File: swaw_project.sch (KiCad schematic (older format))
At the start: 9 parts, among them P1 Power, P2 Analog, P3 Digital, P4 Digital, P5 CONN_01X01, P6 CONN_01X01, P7 CONN_01X01, P8 CONN_01X01

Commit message: Add files via upload
Bluetooth module scheme added to the library of project
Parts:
- added B:HC-05?: Bluetooth_HC-05, symbol swaw_project-cache:Bluetooth_HC-05
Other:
- moved on the sheet: U?
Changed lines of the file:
@@
 L Sensor_Motion:MPU-6050 U?
 U 1 1 5EA88EF4
-P 2900 2150
-F 0 "U?" H 2900 1361 50  0000 C CNN
-F 1 "MPU-6050" H 2900 1270 50  0000 C CNN
-F 2 "Sensor_Motion:InvenSense_QFN-24_4x4mm_P0.5mm" H 2900 1350 50  0001 C CNN
-F 3 "https://store.invensense.com/datasheets/invensense/MPU-6050_DataSheet_V3%204.pdf" H 2900 2000 50  0001 C CNN
-	1    2900 2150
+P 2700 2050
+F 0 "U?" H 2700 1261 50  0000 C CNN
+F 1 "MPU-6050" H 2700 1170 50  0000 C CNN
+F 2 "Sensor_Motion:InvenSense_QFN-24_4x4mm_P0.5mm" H 2700 1250 50  0001 C CNN
+F 3 "https://store.invensense.com/datasheets/invensense/MPU-6050_DataSheet_V3%204.pdf" H 2700 1900 50  0001 C CNN
+	1    2700 2050
 	1    0    0    -1
 $EndComp
+$Comp
+L swaw_project-cache:Bluetooth_HC-05 B:HC-05?
+U 1 1 5EAA6265
+P 5000 2400
+F 0 "B:HC-05?" H 5200 3315 50  0000 C CNN
+F 1 "Bluetooth_HC-05" H 5200 3224 50  0000 C CNN
+F 2 "" H 5000 2400 50  0001 C CNN
+F 3 "" H 5000 2400 50  0001 C CNN
+	1    5000 2400
+	1    0    0    -1
+$EndComp

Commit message: Add files via upload
Adding Bluetooth PIO, capacitors, resistors values and footprints
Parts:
- removed B:HC-05?: Bluetooth_HC-05, symbol swaw_project-cache:Bluetooth_HC-05
- added C1: 10nF, Capacitor_THT:CP_Axial_L11.0mm_D6.0mm_P18.00mm_Horizontal, symbol pspice:C
- added C2, C3: 0.1uF, Capacitor_THT:CP_Axial_L11.0mm_D6.0mm_P18.00mm_Horizontal, symbol pspice:C
- added C4: 2.2nF, Capacitor_THT:CP_Axial_L11.0mm_D6.0mm_P18.00mm_Horizontal, symbol pspice:C
- added HC-05_PIO?: Bluetooh_PIO, Connector_PinHeader_2.54mm:PinHeader_1x06_P2.54mm_Vertical, symbol Relay:Bluetooh_PIO
- added R1, R2: 10kΩ, Resistor_THT:R_Axial_DIN0309_L9.0mm_D3.2mm_P15.24mm_Horizontal, symbol Device:R
- added R3: 2kΩ, Resistor_THT:R_Axial_DIN0309_L9.0mm_D3.2mm_P15.24mm_Horizontal, symbol Device:R
- added R4: 1kΩ, Resistor_THT:R_Axial_DIN0309_L9.0mm_D3.2mm_P15.24mm_Horizontal, symbol Device:R
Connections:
- wire segments 38 -> 98
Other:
- moved on the sheet: U?

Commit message: Added logic shifters for i2c and basic pcb layout
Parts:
- added Q1, Q2: 2N7000, Package_TO_SOT_THT:TO-92_Inline, symbol Transistor_FET:2N7000
- added R5, R6: 10kΩ, Resistor_SMD:R_0612_1632Metric_Pad1.18x3.40mm_HandSolder, symbol Device:R
- C1: footprint Capacitor_THT:CP_Axial_L11.0mm_D6.0mm_P18.00mm_Horizontal -> Capacitor_SMD:C_0805_2012Metric_Pad1.15x1.40mm_HandSolder
- C2, C3: footprint Capacitor_THT:CP_Axial_L11.0mm_D6.0mm_P18.00mm_Horizontal -> Capacitor_SMD:C_1206_3216Metric_Pad1.42x1.75mm_HandSolder
- C4: footprint Capacitor_THT:CP_Axial_L11.0mm_D6.0mm_P18.00mm_Horizontal -> Capacitor_SMD:C_0603_1608Metric_Pad1.05x0.95mm_HandSolder
- HC-05_PIO1: renamed from HC-05_PIO?; symbol Relay:Bluetooh_PIO -> swaw_project-rescue:Bluetooh_PIO-Relay
- R1, R2: footprint Resistor_THT:R_Axial_DIN0309_L9.0mm_D3.2mm_P15.24mm_Horizontal -> Resistor_SMD:R_0612_1632Metric_Pad1.18x3.40mm_HandSolder
- R3: footprint Resistor_THT:R_Axial_DIN0309_L9.0mm_D3.2mm_P15.24mm_Horizontal -> Resistor_SMD:R_0805_2012Metric_Pad1.15x1.40mm_HandSolder
- R4: footprint Resistor_THT:R_Axial_DIN0309_L9.0mm_D3.2mm_P15.24mm_Horizontal -> Resistor_SMD:R_0603_1608Metric_Pad1.05x0.95mm_HandSolder
- gave numbers to parts that had none: 1
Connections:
- wire segments 98 -> 112
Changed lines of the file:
@@
 	10200 1200 10550 1200
-Wire Wire Line
-	10200 3000 10400 3000
 Wire Wire Line
 	10200 2800 10550 2800
@@
 	10700 1000 10700 500
 $Comp
-L Sensor_Motion:MPU-6050 U?
+L Sensor_Motion:MPU-6050 U1
 U 1 1 5EA88EF4
 P 2900 2150
-F 0 "U?" H 2900 1361 50  0000 C CNN
+F 0 "U1" H 2900 1361 50  0000 C CNN
 F 1 "MPU-6050" H 2900 1270 50  0000 C CNN
 F 2 "Sensor_Motion:InvenSense_QFN-24_4x4mm_P0.5mm" H 2900 1350 50  0001 C CNN
@@
 F 0 "C2" H 4078 1646 50  0000 L CNN
 F 1 "0.1uF" H 4078 1555 50  0000 L CNN
-F 2 "Capacitor_THT:CP_Axial_L11.0mm_D6.0mm_P18.00mm_Horizontal" H 3900 1600 50  0001 C CNN
+F 2 "Capacitor_SMD:C_1206_3216Metric_Pad1.42x1.75mm_HandSolder" H 3900 1600 50  0001 C CNN
 F 3 "~" H 3900 1600 50  0001 C CNN
 	1    3900 1600
@@
 	2900 900  2800 900
 $Comp
-L power:GND #PWR?
+L power:GND #PWR08
 U 1 1 5EAAFEC1
 P 3900 1850
-F 0 "#PWR?" H 3900 1600 50  0001 C CNN
+F 0 "#PWR08" H 3900 1600 50  0001 C CNN
 F 1 "GND" H 3905 1677 50  0000 C CNN
 F 2 "" H 3900 1850 50  0001 C CNN
@@
 $EndComp
 $Comp
-L power:GND #PWR?
+L power:GND #PWR06
 U 1 1 5EAB0D0F
 P 2900 1400
-F 0 "#PWR?" H 2900 1150 50  0001 C CNN
+F 0 "#PWR06" H 2900 1150 50  0001 C CNN
 F 1 "GND" H 2905 1227 50  0000 C CNN
 F 2 "" H 2900 1400 50  0001 C CNN
@@
 F 0 "C1" H 3078 1196 50  0000 L CNN
 F 1 "10nF" H 3078 1105 50  0000 L CNN
-F 2 "Capacitor_THT:CP_Axial_L11.0mm_D6.0mm_P18.00mm_Horizontal" H 2900 1150 50  0001 C CNN
+F 2 "Capacitor_SMD:C_0805_2012Metric_Pad1.15x1.40mm_HandSolder" H 2900 1150 50  0001 C CNN
 F 3 "~" H 2900 1150 50  0001 C CNN
 	1    2900 1150
@@
 $EndComp
 $Comp
-L power:GND #PWR?
+L power:GND #PWR07
 U 1 1 5EABDA5F
 P 2900 2850
-F 0 "#PWR?" H 2900 2600 50  0001 C CNN
+F 0 "#PWR07" H 2900 2600 50  0001 C CNN
 F 1 "GND" H 2905 2677 50  0000 C CNN
 F 2 "" H 2900 2850 50  0001 C CNN
@@
 F 0 "C4" H 4778 2646 50  0000 L CNN
 F 1 "2.2nF" H 4778 2555 50  0000 L CNN
-F 2 "Capacitor_THT:CP_Axial_L11.0mm_D6.0mm_P18.00mm_Horizontal" H 4600 2600 50  0001 C CNN
+F 2 "Capacitor_SMD:C_0603_1608Metric_Pad1.05x0.95mm_HandSolder" H 4600 2600 50  0001 C CNN
 F 3 "~" H 4600 2600 50  0001 C CNN
 	1    4600 2600
@@
 F 0 "C3" H 4078 2746 50  0000 L CNN
 F 1 "0.1uF" H 4078 2655 50  0000 L CNN
-F 2 "Capacitor_THT:CP_Axial_L11.0mm_D6.0mm_P18.00mm_Horizontal" H 3900 2700 50  0001 C CNN
+F 2 "Capacitor_SMD:C_1206_3216Metric_Pad1.42x1.75mm_HandSolder" H 3900 2700 50  0001 C CNN
 F 3 "~" H 3900 2700 50  0001 C CNN
 	1    3900 2700
@@
 	3900 2450 3600 2450
 $Comp
-L power:GND #PWR?
+L power:GND #PWR09
 U 1 1 5EAC0805
 P 3900 2950
-F 0 "#PWR?" H 3900 2700 50  0001 C CNN
+F 0 "#PWR09" H 3900 2700 50  0001 C CNN
 F 1 "GND" H 3905 2777 50  0000 C CNN
 F 2 "" H 3900 2950 50  0001 C CNN
@@
 $EndComp
 $Comp
-L power:GND #PWR?
+L power:GND #PWR010
 U 1 1 5EAC0AA7
 P 4600 2850
-F 0 "#PWR?" H 4600 2600 50  0001 C CNN
+F 0 "#PWR010" H 4600 2600 50  0001 C CNN
 F 1 "GND" H 4605 2677 50  0000 C CNN
 F 2 "" H 4600 2850 50  0001 C CNN
@@
 	1650 1950 2200 1950
 $Comp
-L power:GND #PWR?
+L power:GND #PWR05
 U 1 1 5EADDE16
 P 1950 2550
-F 0 "#PWR?" H 1950 2300 50  0001 C CNN
+F 0 "#PWR05" H 1950 2300 50  0001 C CNN
 F 1 "GND" H 1955 2377 50  0000 C CNN
 F 2 "" H 1950 2550 50  0001 C CNN
@@
 F 0 "R2" H 5770 1746 50  0000 L CNN
 F 1 "10kΩ" H 5770 1655 50  0000 L CNN
-F 2 "Resistor_THT:R_Axial_DIN0309_L9.0mm_D3.2mm_P15.24mm_Horizontal" V 5630 1700 50  0001 C CNN
+F 2 "Resistor_SMD:R_0612_1632Metric_Pad1.18x3.40mm_HandSolder" V 5630 1700 50  0001 C CNN
 F 3 "~" H 5700 1700 50  0001 C CNN
 	1    5700 1700
@@
 F 0 "R1" H 5320 1746 50  0000 L CNN
 F 1 "10kΩ" H 5320 1655 50  0000 L CNN
-F 2 "Resistor_THT:R_Axial_DIN0309_L9.0mm_D3.2mm_P15.24mm_Horizontal" V 5180 1700 50  0001 C CNN
+F 2 "Resistor_SMD:R_0612_1632Metric_Pad1.18x3.40mm_HandSolder" V 5180 1700 50  0001 C CNN
 F 3 "~" H 5250 1700 50  0001 C CNN
 	1    5250 1700
@@
 Connection ~ 5700 900
 Wire Wire Line
-	5700 900  9150 900
-Wire Wire Line
 	10200 1300 10700 1300
 Wire Wire Line
@@
 	1450 4050 5250 4050
 Wire Wire Line
-	5250 4050 5250 2700
-Wire Wire Line
 	1650 1950 1650 3900
 Wire Wire Line
 	1650 3900 5700 3900
 Wire Wire Line
-	5700 3900 5700 2000
-Wire Wire Line
 	10550 1200 10550 950
-Wire Wire Line
-	10550 950  6450 950
-Wire Wire Line
-	6450 950  6450 2000
-Wire Wire Line
-	6450 2000 5700 2000
-Connection ~ 5700 2000
-Wire Wire Line
-	5700 2000 5700 1850
-Wire Wire Line
-	10700 1300 10700 1050
-Wire Wire Line
-	10700 1050 6600 1050
-Wire Wire Line
-	6600 1050 6600 2700
-Wire Wire Line
-	6600 2700 5250 2700
-Connection ~ 5250 2700
-Wire Wire Line
-	5250 2700 5250 1850
 Wire Wire Line
 	2200 2050 1950 2050
@@
 Connection ~ 1950 2350
 $Comp
-L Relay:Bluetooh_PIO HC-05_PIO?
+L swaw_project-rescue:Bluetooh_PIO-Relay HC-05_PIO1
 U 1 1 5EAA8D5B
 P 10650 5000
-F 0 "HC-05_PIO?" H 10717 5823 50  0000 C CNN
+F 0 "HC-05_PIO1" H 10717 5823 50  0000 C CNN
 F 1 "Bluetooh_PIO" H 10800 5800 50  0001 C CNN
 F 2 "Connector_PinHeader_2.54mm:PinHeader_1x06_P2.54mm_Vertical" H 10650 5000 50  0001 C CNN
@@
 F 0 "R3" H 10220 4196 50  0000 L CNN
 F 1 "2kΩ" H 10220 4105 50  0000 L CNN
-F 2 "Resistor_THT:R_Axial_DIN0309_L9.0mm_D3.2mm_P15.24mm_Horizontal" V 10080 4150 50  0001 C CNN
+F 2 "Resistor_SMD:R_0805_2012Metric_Pad1.15x1.40mm_HandSolder" V 10080 4150 50  0001 C CNN
 F 3 "~" H 10150 4150 50  0001 C CNN
 	1    10150 4150
@@
 F 0 "R4" H 10470 3946 50  0000 L CNN
 F 1 "1kΩ" H 10470 3855 50  0000 L CNN
-F 2 "Resistor_THT:R_Axial_DIN0309_L9.0mm_D3.2mm_P15.24mm_Horizontal" V 10330 3900 50  0001 C CNN
+F 2 "Resistor_SMD:R_0603_1608Metric_Pad1.05x0.95mm_HandSolder" V 10330 3900 50  0001 C CNN
 F 3 "~" H 10400 3900 50  0001 C CNN
 	1    10400 3900
@@
 $EndComp
 Wire Wire Line
-	10200 2900 10500 2900
-Wire Wire Line
 	10500 4850 7900 4850
 Wire Wire Line
-	7900 4850 7900 1350
-Wire Wire Line
-	7900 1350 9050 1350
+	7900 4850 7900 1400
+Wire Wire Line
+	7900 1350 7950 1350
 Connection ~ 9050 1350
 Wire Wire Line
@@
 	10400 4550 10400 4150
 Wire Wire Line
-	10400 3750 10400 3000
-Connection ~ 10400 3000
-Wire Wire Line
-	10400 3000 10550 3000
-Wire Wire Line
 	10400 4150 10300 4150
 Connection ~ 10400 4150
@@
 	9650 4650 9650 3600
 Wire Wire Line
-	9650 3600 10500 3600
-Wire Wire Line
-	10500 3600 10500 2900
-Connection ~ 10500 2900
-Wire Wire Line
-	10500 2900 10600 2900
+	10200 3000 10550 3000
+Wire Wire Line
+	10200 2900 10600 2900
+Wire Wire Line
+	10400 3750 10600 3750
+Wire Wire Line
+	10600 3750 10600 2900
+Wire Wire Line
+	10550 3000 10550 3600
+Wire Wire Line
+	10550 3600 9650 3600
+$Comp
+L Transistor_FET:2N7000 Q1
+U 1 1 5EABA114
+P 6400 1200
+F 0 "Q1" V 6649 1200 50  0000 C CNN
+F 1 "2N7000" V 6740 1200 50  0000 C CNN
+F 2 "Package_TO_SOT_THT:TO-92_Inline" H 6600 1125 50  0001 L CIN
+F 3 "https://www.fairchildsemi.com/datasheets/2N/2N7000.pdf" H 6400 1200 50  0001 L CNN
+	1    6400 1200
+	0    1    1    0
+$EndComp
+$Comp
+L Transistor_FET:2N7000 Q2
+U 1 1 5EABADA7
+P 7000 1600
+F 0 "Q2" V 7249 1600 50  0000 C CNN
+F 1 "2N7000" V 7340 1600 50  0000 C CNN
+F 2 "Package_TO_SOT_THT:TO-92_Inline" H 7200 1525 50  0001 L CIN
+F 3 "https://www.fairchildsemi.com/datasheets/2N/2N7000.pdf" H 7000 1600 50  0001 L CNN
+	1    7000 1600
+	0    1    1    0
+$EndComp
+Wire Wire Line
+	5250 1850 5250 1900
+Wire Wire Line
+	5700 1850 5700 2100
+Connection ~ 7000 900
+Wire Wire Line
+	7000 900  9150 900
+Wire Wire Line
+	5700 900  6400 900
+Wire Wire Line
+	6400 1000 6400 900
+Connection ~ 6400 900
+Wire Wire Line
+	6400 900  7000 900
+Wire Wire Line
+	5250 1900 6200 1900
+Wire Wire Line
+	6200 1900 6200 1300
+Connection ~ 5250 1900
+Wire Wire Line
+	5250 1900 5250 4050
+Wire Wire Line
+	5700 2100 6800 2100
+Wire Wire Line
+	6800 2100 6800 1700
+Connection ~ 5700 2100
+Wire Wire Line
+	5700 2100 5700 3900
+Wire Wire Line
+	7000 900  7000 1400
+$Comp
+L Device:R R5
+U 1 1 5EAF622B
+P 7300 1150
+F 0 "R5" H 7370 1196 50  0000 L CNN
+F 1 "10kΩ" H 7370 1105 50  0000 L CNN
+F 2 "Resistor_SMD:R_0612_1632Metric_Pad1.18x3.40mm_HandSolder" V 7230 1150 50  0001 C CNN
+F 3 "~" H 7300 1150 50  0001 C CNN
+	1    7300 1150
+	1    0    0    -1
+$EndComp
+$Comp
+L Device:R R6
+U 1 1 5EAF6BDC
+P 7400 1550
+F 0 "R6" H 7470 1596 50  0000 L CNN
+F 1 "10kΩ" H 7470 1505 50  0000 L CNN
+F 2 "Resistor_SMD:R_0612_1632Metric_Pad1.18x3.40mm_HandSolder" V 7330 1550 50  0001 C CNN
+F 3 "~" H 7400 1550 50  0001 C CNN
+	1    7400 1550
+	1    0    0    -1
+$EndComp
+Wire Wire Line
+	7200 1700 7400 1700
+Wire Wire Line
+	6600 1300 7300 1300
+Wire Wire Line
+	7300 1000 7950 1000
+Wire Wire Line
+	7950 1000 7950 1350
+Connection ~ 7950 1350
+Wire Wire Line
+	7950 1350 9050 1350
+Wire Wire Line
+	7400 1400 7900 1400
+Connection ~ 7900 1400
+Wire Wire Line
+	7900 1400 7900 1350
+Wire Wire Line
+	7300 1300 9500 1300
+Wire Wire Line
+	9500 1300 9500 850
+Wire Wire Line
+	9500 850  10700 850
+Wire Wire Line
+	10700 850  10700 1300
+Connection ~ 7300 1300
+Wire Wire Line
+	7400 1700 8700 1700
+Wire Wire Line
+	8700 1700 8700 950
+Wire Wire Line
+	8700 950  10550 950
+Connection ~ 7400 1700
 $EndSCHEMATC

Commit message: Add files via upload
Removing right angles for paths
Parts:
- HC-05_PIO1: footprint Connector_PinHeader_2.54mm:PinHeader_1x06_P2.54mm_Vertical -> Connector_PinSocket_2.54mm:PinSocket_1x06_P2.54mm_Vertical
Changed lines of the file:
@@
 F 0 "HC-05_PIO1" H 10717 5823 50  0000 C CNN
 F 1 "Bluetooh_PIO" H 10800 5800 50  0001 C CNN
-F 2 "Connector_PinHeader_2.54mm:PinHeader_1x06_P2.54mm_Vertical" H 10650 5000 50  0001 C CNN
+F 2 "Connector_PinSocket_2.54mm:PinSocket_1x06_P2.54mm_Vertical" H 10650 5000 50  0001 C CNN
 F 3 "" H 10650 5000 50  0001 C CNN
 	1    10650 5000

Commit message: Adding changes to layout after review
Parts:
- added R7, R8: 100Ω, Resistor_SMD:R_0603_1608Metric_Pad1.05x0.95mm_HandSolder, symbol Device:R
- C1: value 10nF -> 110nF
- Q1, Q2: value 2N7000 -> 2N7002; footprint Package_TO_SOT_THT:TO-92_Inline -> Package_TO_SOT_SMD:SOT-23; symbol Transistor_FET:2N7000 -> Transistor_FET:2N7002
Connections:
- net +3V3: now also Q1.1 (G), Q2.1 (G); no longer Q1.2 (G), Q2.2 (G)
- net 0(Rx): now also R4.1; no longer HC-05_PIO1.4 (TXD)
- net 1(Tx): now also R7.1; no longer R4.1
- net GND: now also R3.2; no longer R3.1
- net at R2.2, U1.23 (SCL): now also Q2.2 (S); no longer Q2.1 (S)
- net at R1.2, U1.24 (SDA): now also Q1.2 (S); no longer Q1.1 (S)
- new net: HC-05_PIO1.3 (RXD), R8.2
- new net: HC-05_PIO1.4 (TXD), R7.2
- new net: R3.1, R4.2, R8.1
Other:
- moved on the sheet: C1, Q1, Q2, R1, R2, R3, R4, R5, R6

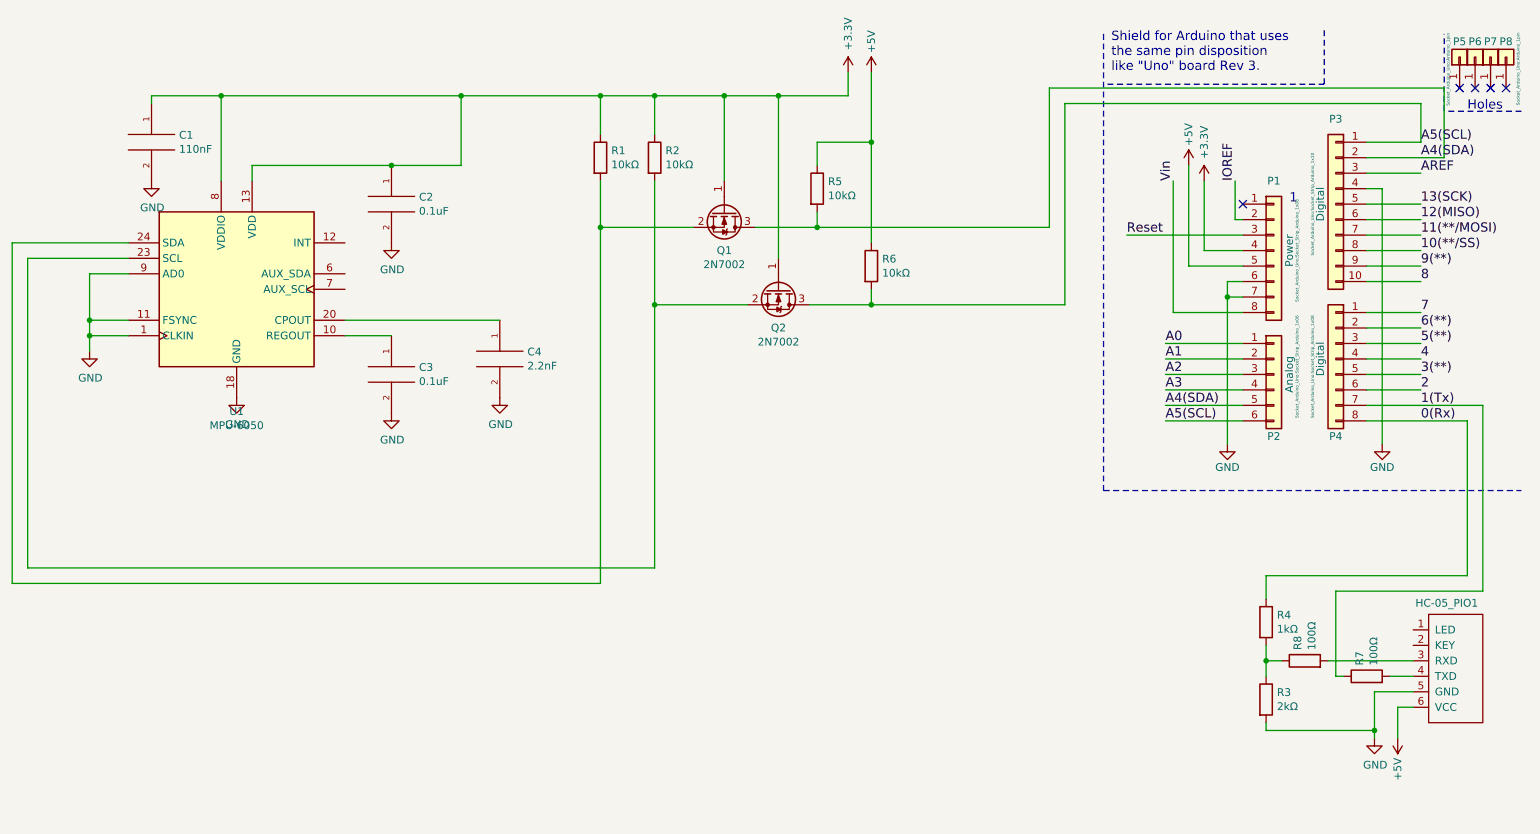
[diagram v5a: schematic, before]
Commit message: Fixed tx/rx connection, added gnd planes and some vias
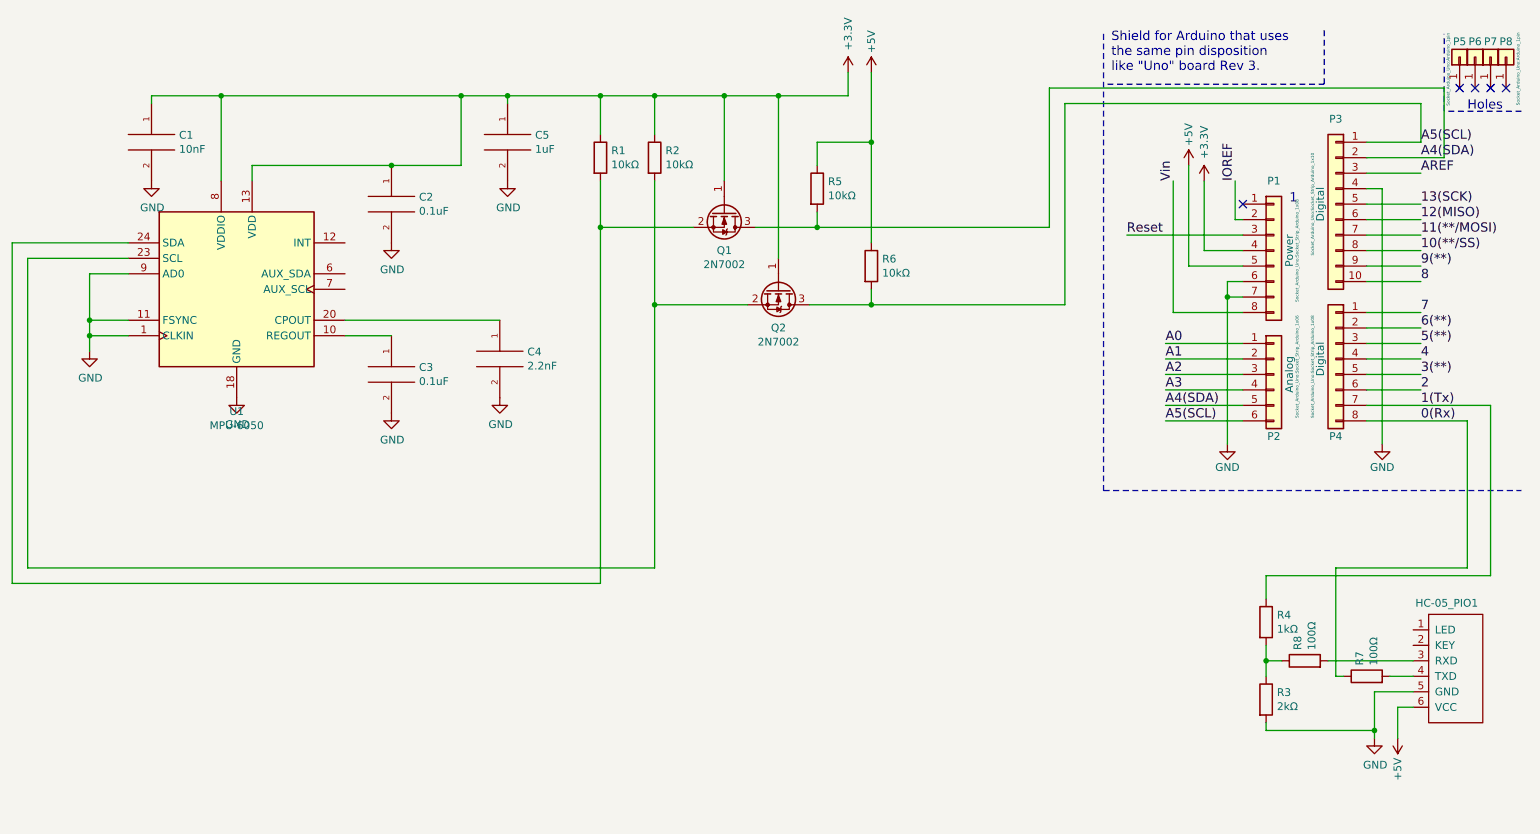
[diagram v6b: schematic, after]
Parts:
- added C5: 1uF, Capacitor_SMD:C_1206_3216Metric_Pad1.42x1.75mm_HandSolder, symbol pspice:C
- C1: value 110nF -> 10nF
- R4: footprint Resistor_SMD:R_0603_1608Metric_Pad1.05x0.95mm_HandSolder -> Resistor_SMD:R_0805_2012Metric_Pad1.15x1.40mm_HandSolder
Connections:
- net +3V3: now also C5.1
- net 0(Rx): now also R7.1; no longer R4.1
- net 1(Tx): now also R4.1; no longer R7.1
- net GND: now also C5.2
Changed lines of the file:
@@
 	10200 1200 10550 1200
-Wire Wire Line
-	10200 2800 10550 2800
 Wire Wire Line
 	10200 2700 10550 2700
@@
 F 0 "R4" H 9620 4346 50  0000 L CNN
 F 1 "1kΩ" H 9620 4255 50  0000 L CNN
-F 2 "Resistor_SMD:R_0603_1608Metric_Pad1.05x0.95mm_HandSolder" V 9480 4300 50  0001 C CNN
+F 2 "Resistor_SMD:R_0805_2012Metric_Pad1.15x1.40mm_HandSolder" V 9480 4300 50  0001 C CNN
 F 3 "~" H 9550 4300 50  0001 C CNN
 	1    9550 4300
@@
 	10050 4650 10000 4650
 Wire Wire Line
-	10000 4650 10000 4100
-Wire Wire Line
-	10000 4100 10950 4100
-Wire Wire Line
-	10950 4100 10950 2900
-Wire Wire Line
-	10200 2900 10950 2900
-Wire Wire Line
 	9650 4550 9550 4550
 Wire Wire Line
@@
 Wire Wire Line
 	9550 4150 9550 4000
-Wire Wire Line
-	9550 4000 10850 4000
-Wire Wire Line
-	10850 4000 10850 3000
 Wire Wire Line
 	10200 3000 10850 3000
@@
 P 2350 1200
 F 0 "C1" H 2528 1246 50  0000 L CNN
-F 1 "110nF" H 2528 1155 50  0000 L CNN
+F 1 "10nF" H 2528 1155 50  0000 L CNN
 F 2 "Capacitor_SMD:C_0805_2012Metric_Pad1.15x1.40mm_HandSolder" H 2350 1200 50  0001 C CNN
 F 3 "~" H 2350 1200 50  0001 C CNN
@@
 Connection ~ 4350 900
 Wire Wire Line
-	4350 900  5250 900
+	4350 900  4650 900
 Connection ~ 5600 900
 Wire Wire Line
@@
 	8250 2250 7000 2250
 Connection ~ 7000 2250
+$Comp
+L power:GND #PWR011
+U 1 1 5EACA0F8
+P 4650 1450
+F 0 "#PWR011" H 4650 1200 50  0001 C CNN
+F 1 "GND" H 4655 1277 50  0000 C CNN
+F 2 "" H 4650 1450 50  0001 C CNN
+F 3 "" H 4650 1450 50  0001 C CNN
+	1    4650 1450
+	1    0    0    -1
+$EndComp
+$Comp
+L pspice:C C5
+U 1 1 5EACB41C
+P 4650 1200
+F 0 "C5" H 4828 1246 50  0000 L CNN
+F 1 "1uF" H 4828 1155 50  0000 L CNN
+F 2 "Capacitor_SMD:C_1206_3216Metric_Pad1.42x1.75mm_HandSolder" H 4650 1200 50  0001 C CNN
+F 3 "~" H 4650 1200 50  0001 C CNN
+	1    4650 1200
+	1    0    0    -1
+$EndComp
+Wire Wire Line
+	4650 900  4650 950
+Connection ~ 4650 900
+Wire Wire Line
+	4650 900  5250 900
+Wire Wire Line
+	11000 4000 11000 2900
+Wire Wire Line
+	9550 4000 11000 4000
+Wire Wire Line
+	10200 2900 11000 2900
+Wire Wire Line
+	10850 3000 10850 3950
+Wire Wire Line
+	10850 3950 10000 3950
+Wire Wire Line
+	10000 3950 10000 4650
+Wire Wire Line
+	10200 2800 10550 2800
 $EndSCHEMATC
